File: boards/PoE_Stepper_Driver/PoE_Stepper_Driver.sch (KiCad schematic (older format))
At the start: 40 parts, among them J4 Programming, J5 48V In, J6 12V, 3V3 Out, J7 PHY Data, J8 SPI Data, J9 UART, SW3 SW_Push, U3 STM32F407VETx, U4 NCP1117, U5 E48SC12010, Y1 8MHz

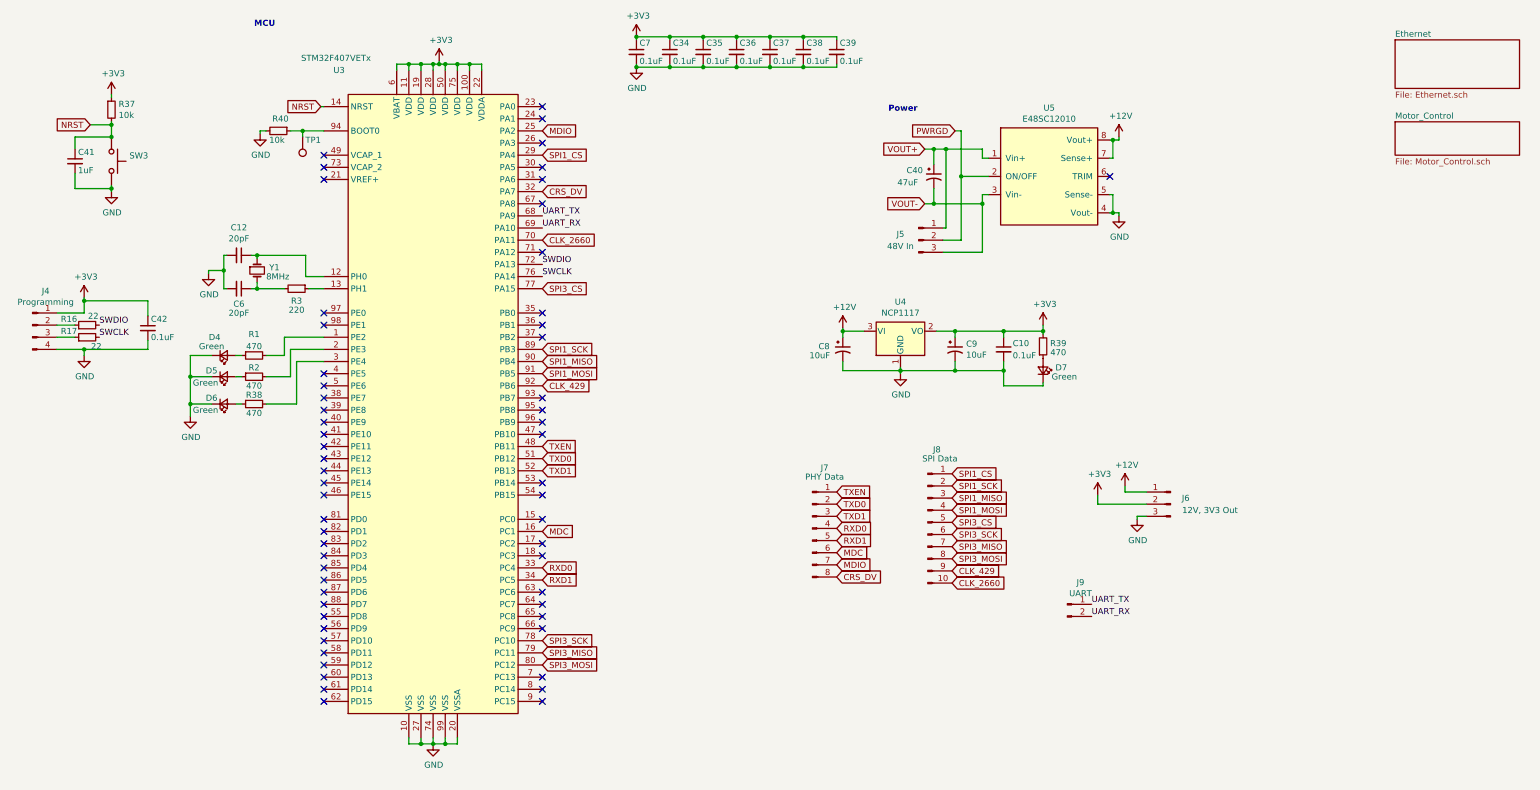
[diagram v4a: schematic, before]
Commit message: made rev2 board changes
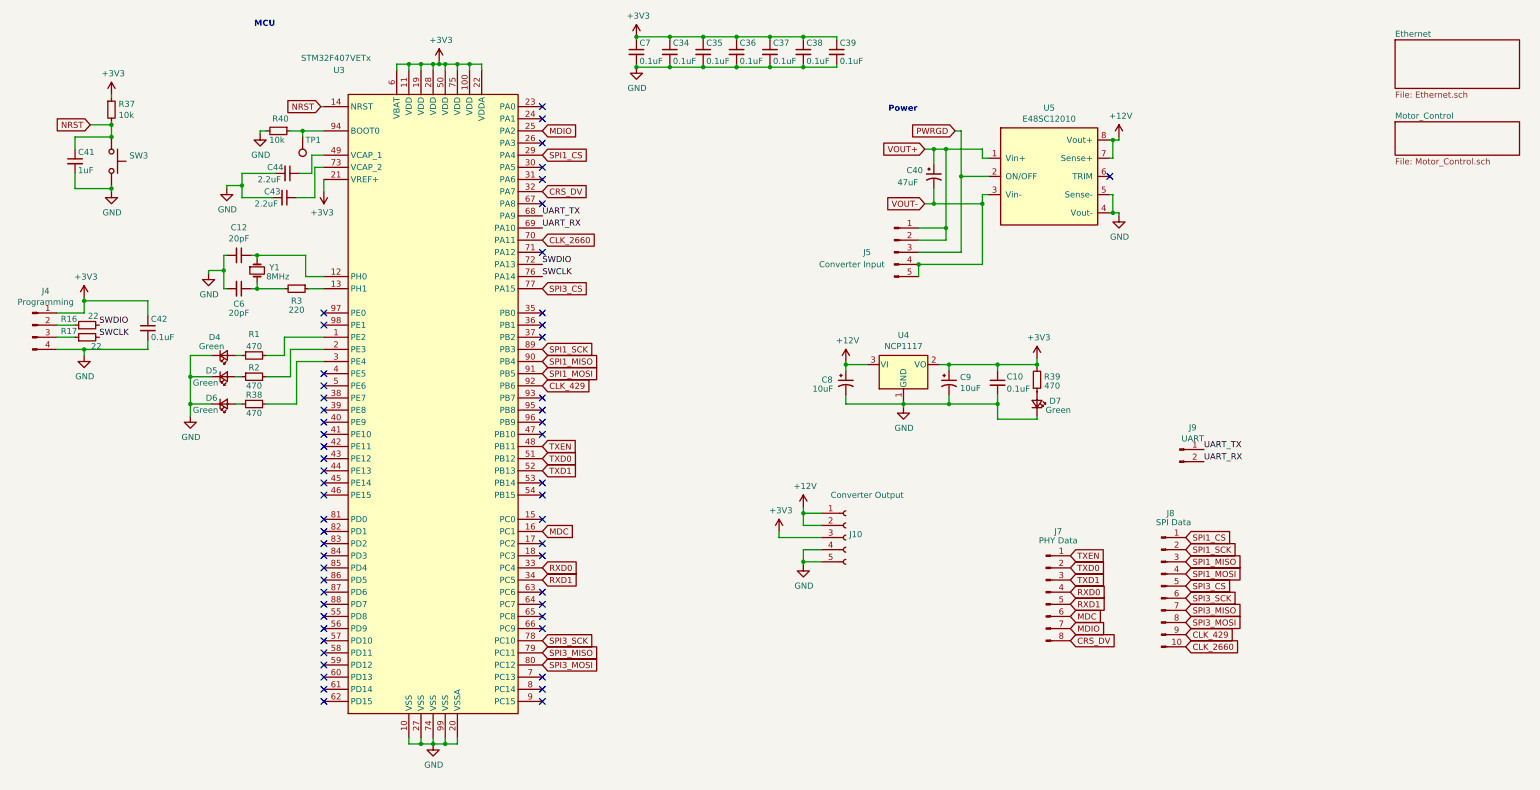
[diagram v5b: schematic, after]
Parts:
- removed J5: 48V In, Connector_PinHeader_2.54mm:PinHeader_1x03_P2.54mm_Vertical, symbol Connector:Conn_01x03_Male
- removed J6: 12V, 3V3 Out, Connector_PinHeader_2.54mm:PinHeader_1x03_P2.54mm_Vertical, symbol Connector:Conn_01x03_Male
- added C43, C44: 2.2uF, Capacitor_SMD:C_0603_1608Metric_Pad1.05x0.95mm_HandSolder, symbol device:C_Small
- added J10: Converter Output, Connector_PinHeader_2.54mm:PinHeader_1x05_P2.54mm_Vertical, symbol Connector:Conn_01x05_Female
- added J5: Converter Input, Connector_PinHeader_2.54mm:PinHeader_1x05_P2.54mm_Vertical, symbol Connector:Conn_01x05_Male
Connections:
- net +12V: now also J10.1 (Pin_1), J10.2 (Pin_2)
- net +3V3: now also U3.21 (VREF+), J10.3 (Pin_3)
- net GND: now also C43.2, C44.2, J10.4 (Pin_4), J10.5 (Pin_5)
- net PWRGD: now also J5.3 (Pin_3)
- net VOUT+: now also J5.1 (Pin_1), J5.2 (Pin_2)
- net VOUT-: now also J5.4 (Pin_4), J5.5 (Pin_5)
- net at U3.49 (VCAP_1): now also C44.1
- net at U3.73 (VCAP_2): now also C43.1
- no-connect marks 59 -> 56
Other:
- moved on the sheet: C10, C8, C9, D7, J7, J8, J9, R39, U4

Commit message: writing to 429 is working
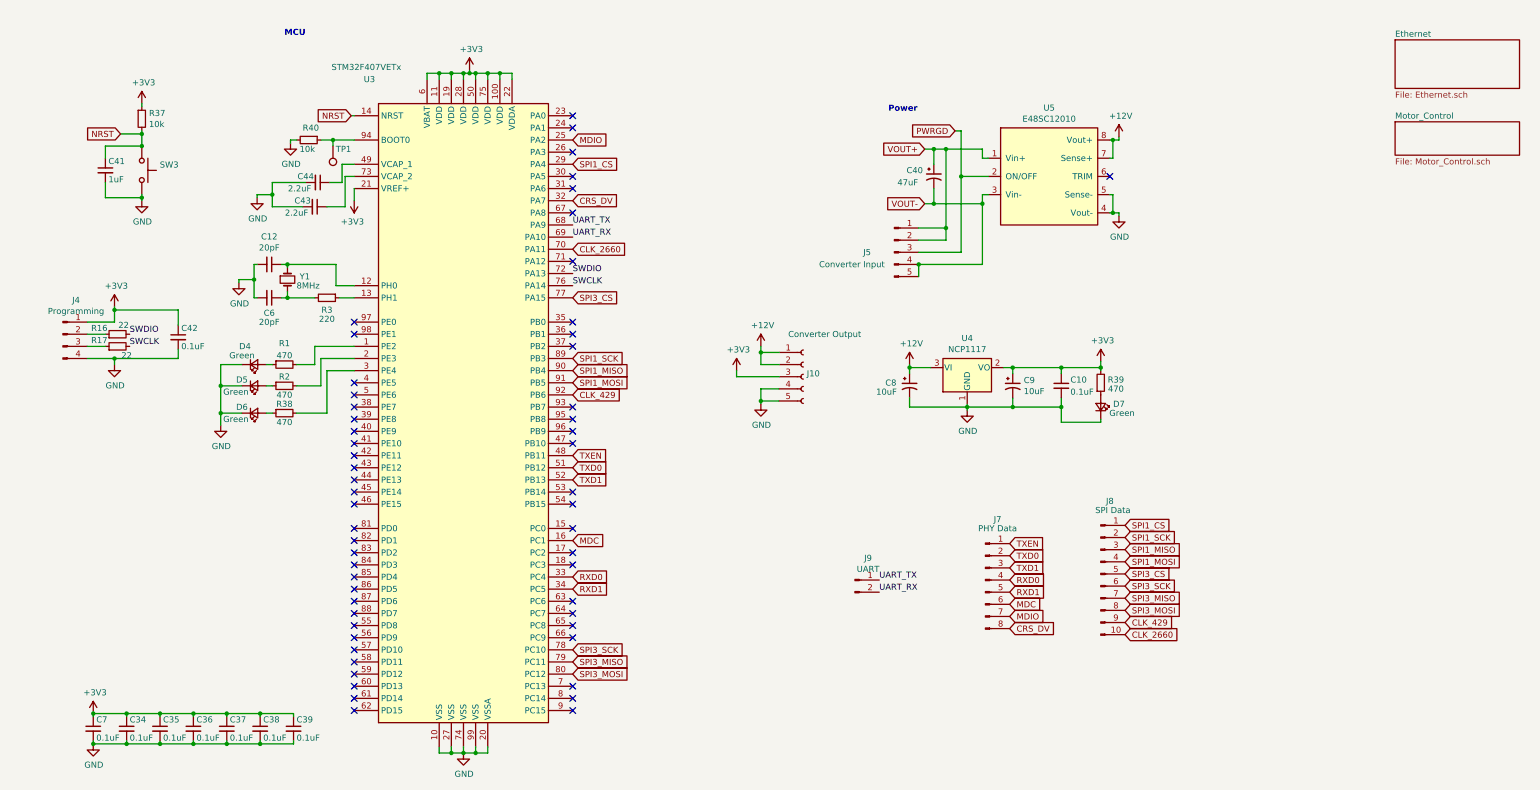
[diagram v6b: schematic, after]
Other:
- moved on the sheet: C10, C12, C34, C35, C36, C37, C38, C39, C41, C42, C43, C44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
